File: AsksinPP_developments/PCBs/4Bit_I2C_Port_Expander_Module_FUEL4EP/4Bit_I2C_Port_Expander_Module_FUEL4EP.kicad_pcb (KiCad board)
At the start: 2 copper layers, 30.5 x 17 mm, 22 parts, among them J1 Conn_01x04, J2 Conn_01x04, J3 Conn_01x04, J4 Conn_01x04, Q1 2N7000, Q2 2N7000, Q3 2N7000, Q4 2N7000, U1 PCA9536D

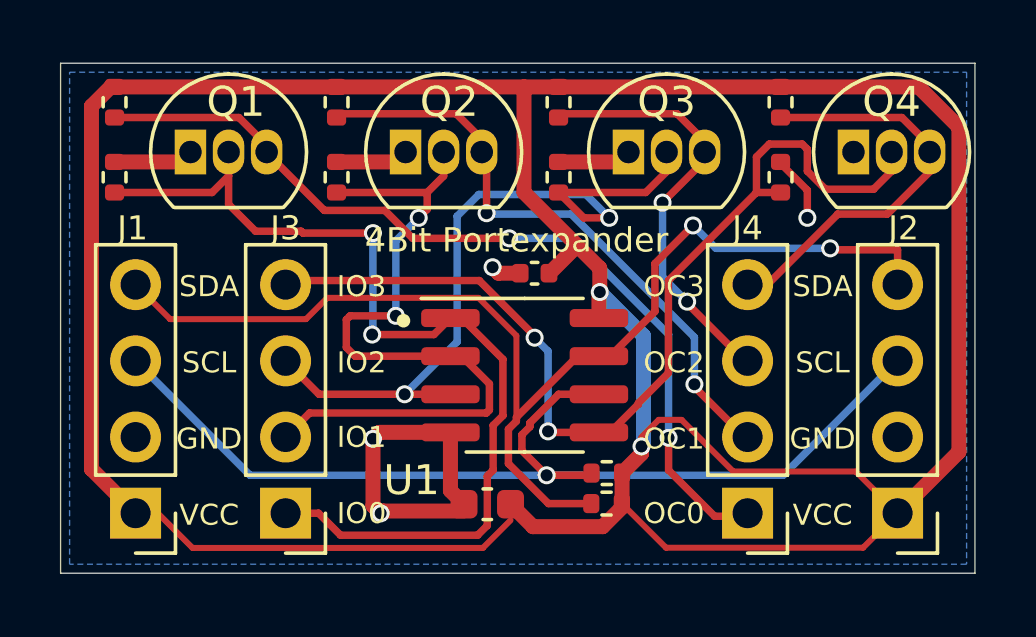
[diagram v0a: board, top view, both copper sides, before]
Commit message: PCB: I2C_Module_SHT85_BME280_FUEL4EP, I2C_Module_BME680_FUEL4EP: correction of connector placements in 3D view; 4Bit_I2C_Port_Expander_Module_FUEL4EP: change from 2N7000 to 2N7002K for SMD assembly
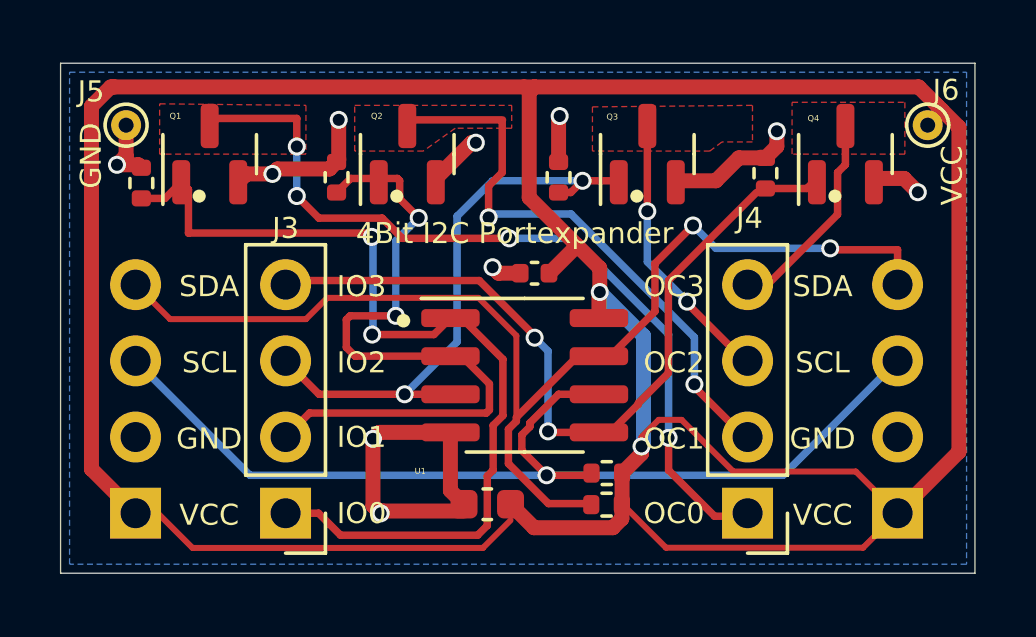
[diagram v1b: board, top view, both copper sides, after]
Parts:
- removed R10, R4, R6, R8: 10k, Resistor_SMD:R_0402_1005Metric
- added J5: Conn_01x01, TestPoint:TestPoint_THTPad_D1.0mm_Drill0.5mm, F.Cu at (2.18, -14.9)
- added J6: Conn_01x01, TestPoint:TestPoint_THTPad_D1.0mm_Drill0.5mm, F.Cu at (28.9, -14.9)
- J1, J2: moved to B.Cu
- Q1, Q2, Q3, Q4: value 2N7000 -> 2N7002K; footprint Package_TO_SOT_THT:TO-92_Inline -> FUEL4EP:SOT-23_2N7002K
- moved R3 0.91 mm to (2.69, -13.0)
- moved Q1 0.64 mm to (4.97, -14.0), turned to 90 degrees
- moved Q3 0.63 mm to (19.6, -14.0), turned to 90 degrees
- moved R9 0.52 mm to (23.5, -13.3)
- moved Q4 0.28 mm to (26.2, -14.0), turned to 90 degrees
- moved Q2 0.09 mm to (11.6, -14.0), turned to 90 degrees
- turned R2 to 0 degrees
- turned J1 to 0 degrees
- turned J2 to 0 degrees
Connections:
- Q1 pad 1: GND -> /IO0
- Q1 pad 2: /IO0 -> GND
- Q2 pad 1: GND -> /IO1
- Q2 pad 2: /IO1 -> GND
- Q3 pad 1: GND -> /IO2
- Q3 pad 2: /IO2 -> GND
- Q4 pad 1: GND -> /IO3
- Q4 pad 2: /IO3 -> GND
- R2 pad 1: VCC -> /SDA
- R2 pad 2: /SDA -> VCC
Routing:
- net GND: track 21.4 -> 28.3 mm, vias 4 -> 10
- net /IO3: track 32.6 -> 25.9 mm
- net /OC3: track 13.1 -> 6.63 mm
- net /IO2: track 24.7 -> 19.2 mm
- net /OC2: track 13.7 -> 9.44 mm
- net /IO1: track 24.7 -> 23.0 mm
- net /IO0: track 32.0 -> 30.4 mm
- net /OC0: track 29.2 -> 27.7 mm, vias 2 -> 4
- net VCC: track 113.3 -> 114.4 mm
- net /OC1: track 19.7 -> 19.2 mm
- added copper zone on F.Cu, net /OC0
- added copper zone on F.Cu, net /OC1
- added copper zone on F.Cu, net /OC2
- added copper zone on F.Cu, net /OC3
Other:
- board text added: "4Bit I2C Portexpander"
- board text added: "4Bit I2C Portexpander (C) FUEL4EP V1.1 12/2023"
- board text removed: "4Bit I2C Portexpander (C) FUEL4EP V1.0 9/2023"
- board text removed: "4Bit Portexpander"

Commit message: PCBs/4Bit_I2C_Port_Expander_Module_FUEL4EP: migration to KiCAD 8
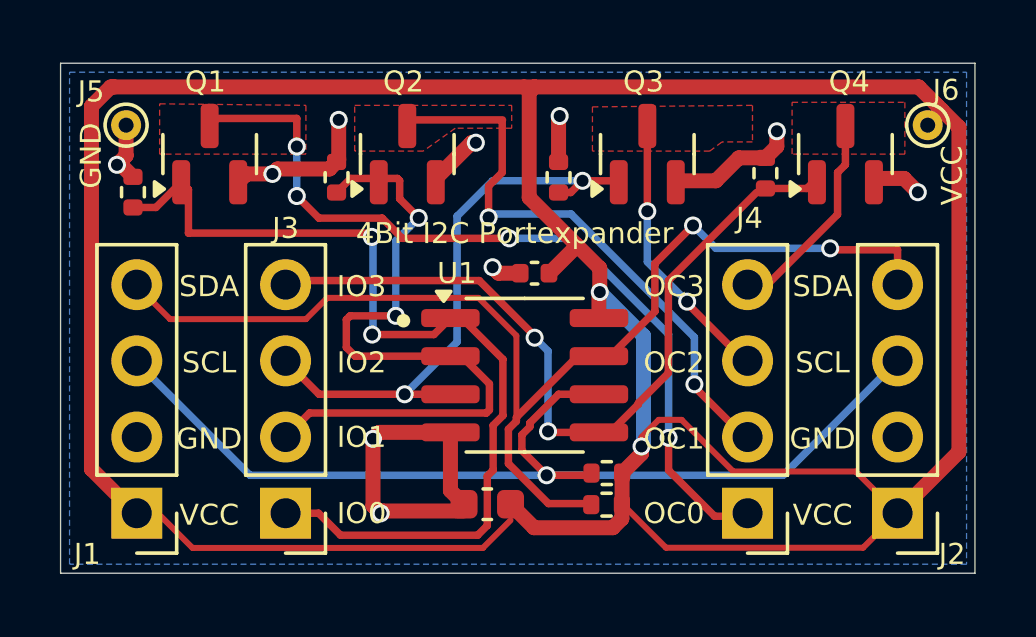
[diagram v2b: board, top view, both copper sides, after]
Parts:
- J1, J2: moved to F.Cu
- Q1, Q2, Q3, Q4: footprint FUEL4EP:SOT-23_2N7002K -> Package_TO_SOT_SMD:SOT-23
- moved R3 0.41 mm to (2.41, -12.7)
- turned J1 to 180 degrees
- turned J2 to 180 degrees
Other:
- board text added: "4Bit I2C Portexpander (C) FUEL4EP V1.2 09/2024"
- board text removed: "4Bit I2C Portexpander (C) FUEL4EP V1.1 12/2023"
